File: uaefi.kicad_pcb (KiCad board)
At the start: 4 copper layers, 100 x 100 mm, 159 parts, among them J1 Conn_02x02_Odd_Even, J10 5569-16A2, J11 Conn_02x02_Odd_Even, J12 Conn_02x02_Odd_Even, J13 Conn_02x02_Odd_Even, J14 Conn_02x02_Odd_Even, J15 Conn_02x02_Odd_Even, J16 Conn_02x02_Odd_Even, J17 Conn_02x02_Odd_Even, J18 Conn_02x02_Odd_Even, J19 Conn_02x02_Odd_Even, J2 5569-20A2, J20 Conn_02x02_Odd_Even, J21 Conn_02x02_Odd_Even, J22 Conn_02x02_Odd_Even, J24 Conn_02x02_Odd_Even, J3 5569-06A2, J4 5569-08A2, J5 5569-18A2, J6 Conn_01x06, J7 Conn_01x05_Male, J8 USB_B_Mini, J9 USB_C, M1 Module-power_12and5V-0.2, M2 Module-knock-0.2, M3 Module-vr-discrete-0.5, M4 Module-vr-max9924-0.1, M5 Module-wbo-0.5, M6 Module:mega-mcu100/0.3, M7 Module-can-0.1, P1 Pad, P15 Pad, P16 Pad, P17 Pad, P18 Pad, P2 Pad, P3 Pad, P4 Pad, P5 Pad, P6 Pad, P7 Pad, P8 Pad, Q10 ISL9V3040D3ST, Q11 ISL9V3040D3ST, Q12 ISL9V3040D3ST, Q7 ISL9V3040D3ST, Q8 ISL9V3040D3ST, Q9 ISL9V3040D3ST, U1 TLE9201SG, U10 VNLD5160TR-E, U11 VNLD5160TR-E, U2 TLE9201SG, U3 MPX4/MPXH6400_MAP, U4 MAX31855KASA, U5 JDY-33, U6 VNLD5160TR-E, U7 VNLD5160TR-E, U8 VNLD5160TR-E, U9 VNLD5160TR-E

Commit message: Prepared the PCB for changes.
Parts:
- removed R5: 0, hellen-one-common:R0603
- moved R29 127.4 mm to (-25.3, 217.7)
- moved R31 127.4 mm to (-27.0, 217.7)
- moved R34 127.4 mm to (-23.6, 217.7)
- moved U10 127.4 mm to (-26.4, 200.0)
- moved U11 127.4 mm to (-26.4, 208.6)
- moved U9 127.4 mm to (-26.4, 191.2)
- moved R30 126.1 mm to (-15.1, 209.1)
- moved R32 126.1 mm to (-17.4, 206.8)
- moved R33 126.1 mm to (-19.2, 207.2)
- moved U5 122.7 mm to (265.2, 145.0)
- moved F10 121.4 mm to (28.9, 189.8)
- moved P7 116.8 mm to (249.4, 148.0)
- moved P8 116.8 mm to (249.4, 152.7)
- moved C27 112.7 mm to (223.0, 76.6)
- moved U3 105.7 mm to (230.2, 78.0)
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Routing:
- net +12V_RAW: track 250.7 -> 0.00 mm, vias 2 -> 0
- net +5VP: track 199.7 -> 0.00 mm, vias 3 -> 0
- net +5VA: track 171.8 -> 0.00 mm, vias 6 -> 0
- net +3.3VA: track 169.4 -> 0.00 mm, vias 5 -> 0
- net GNDA: track 155.8 -> 0.00 mm, vias 5 -> 0
- net /LS_HOT1: track 140.6 -> 0.13 mm, vias 2 -> 0
- net /LS_HOT2: track 138.9 -> 0.00 mm, vias 2 -> 0
- net /EGT/SPI_CS: track 111.5 -> 0.00 mm, vias 1 -> 0
- net /IN_BUTTON3: track 109.6 -> 0.00 mm, vias 1 -> 0
- net +3.3V: track 108.0 -> 0.00 mm, vias 8 -> 0
- net /EGT/SPI_SCK: track 107.3 -> 0.00 mm, vias 1 -> 0
- net /EGT/SPI_SO: track 104.7 -> 0.00 mm, vias 1 -> 0
- net /CAN+: track 102.6 -> 0.00 mm
- net /CAN-: track 100.8 -> 0.00 mm
- net /INJ1: track 89.1 -> 0.00 mm, vias 3 -> 0
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- removed copper zone on B.Cu, net /DC Driver 1/PWR
- removed copper zone on B.Cu, net /DC Driver 2/PWR
- removed copper zone on B.Cu, net GND
- removed copper zone on F.Cu, net GND
- removed copper zone on In1.Cu, net GND
- removed copper zone on In2.Cu, net GND
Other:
- board size 100 x 100 mm -> 150 x 120 mm
- copper layers 4 -> 2
- board text removed: "Always looking for C/C++/PHP/Java developers https://rusefi.com/s/mission"
- board text removed: "COMMUNITY SUPPORT ECU"
- board text removed: "G"
- board text removed: "https://rusefi.com/s/uaefi"

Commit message: tyring to make the pcb a two layer board
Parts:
- added R5: 0, hellen-one-common:R0603, F.Cu at (114.0, 88.0)
- BT1, D2, D4, R12, R13, R15, R16, U6, U8: moved to F.Cu
- moved U9 132.9 mm to (54.6, 85.9)
- moved U10 132.9 mm to (54.6, 94.6)
- moved R34 132.8 mm to (61.0, 115.3), turned to -90 degrees
- moved U11 132.7 mm to (54.6, 103.5)
- moved R31 132.5 mm to (57.1, 115.3), turned to -90 degrees
- moved R29 129.8 mm to (54.6, 115.3), turned to -90 degrees
- moved R33 121.1 mm to (59.7, 115.3)
- moved R32 118.8 mm to (58.4, 115.3)
- moved R30 117.5 mm to (55.9, 115.3), turned to -90 degrees
- moved C27 91.2 mm to (132.0, 83.0), turned to 0 degrees
- moved F10 90.4 mm to (84.5, 118.5)
- moved F5 90.4 mm to (84.5, 90.5)
- moved F6 90.4 mm to (84.5, 83.5)
- moved F7 90.4 mm to (84.6, 97.5)
- moved F8 90.4 mm to (84.6, 104.5)
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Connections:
- J20 pad 3: /OUT_IGN5 -> /OUT_IGN3
- J21 pad 1: /OUT_IGN3 -> /OUT_IGN4
- J21 pad 3: /OUT_IGN4 -> /OUT_IGN5
- J5 pad 11: /OUT_IGN4 -> /OUT_IGN5
- J5 pad 12: /OUT_IGN3 -> /OUT_IGN4
- J5 pad 13: /OUT_IGN5 -> /OUT_IGN3
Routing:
- net /INJ1: track 0.00 -> 120.2 mm, vias 0 -> 2
- net /INJ2: track 0.00 -> 119.7 mm, vias 0 -> 2
- net /INJ4: track 0.00 -> 108.5 mm, vias 0 -> 2
- net /INJ3: track 0.35 -> 108.7 mm, vias 0 -> 2
- net /INJ5: track 0.00 -> 98.0 mm, vias 0 -> 2
- net /INJ6: track 0.14 -> 95.4 mm, vias 0 -> 2
- net /OUT_DC2+: track 0.00 -> 27.8 mm
- net /OUT_DC1+: track 0.00 -> 24.9 mm, vias 0 -> 2
- net /OUT_DC2-: track 0.00 -> 22.2 mm, vias 0 -> 2
- net +12V: track 0.00 -> 21.1 mm
- net /12V_KEY: track 0.00 -> 20.8 mm
- net /DC Driver 1/PWR: track 0.00 -> 14.5 mm, vias 0 -> 2
- net /OUT_IGN6: track 0.00 -> 12.3 mm
- net /OUT_IGN2: track 0.00 -> 11.4 mm
- net /OUT_IGN5: track 0.00 -> 10.8 mm
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- added copper zone on B.Cu, net /DC Driver 1/PWR
- added copper zone on B.Cu, net /DC Driver 2/PWR
- added copper zone on F.Cu, net /OUT_IGN1
- added copper zone on F.Cu, net /OUT_IGN3
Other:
- board text removed: "UAEFI rev. D"

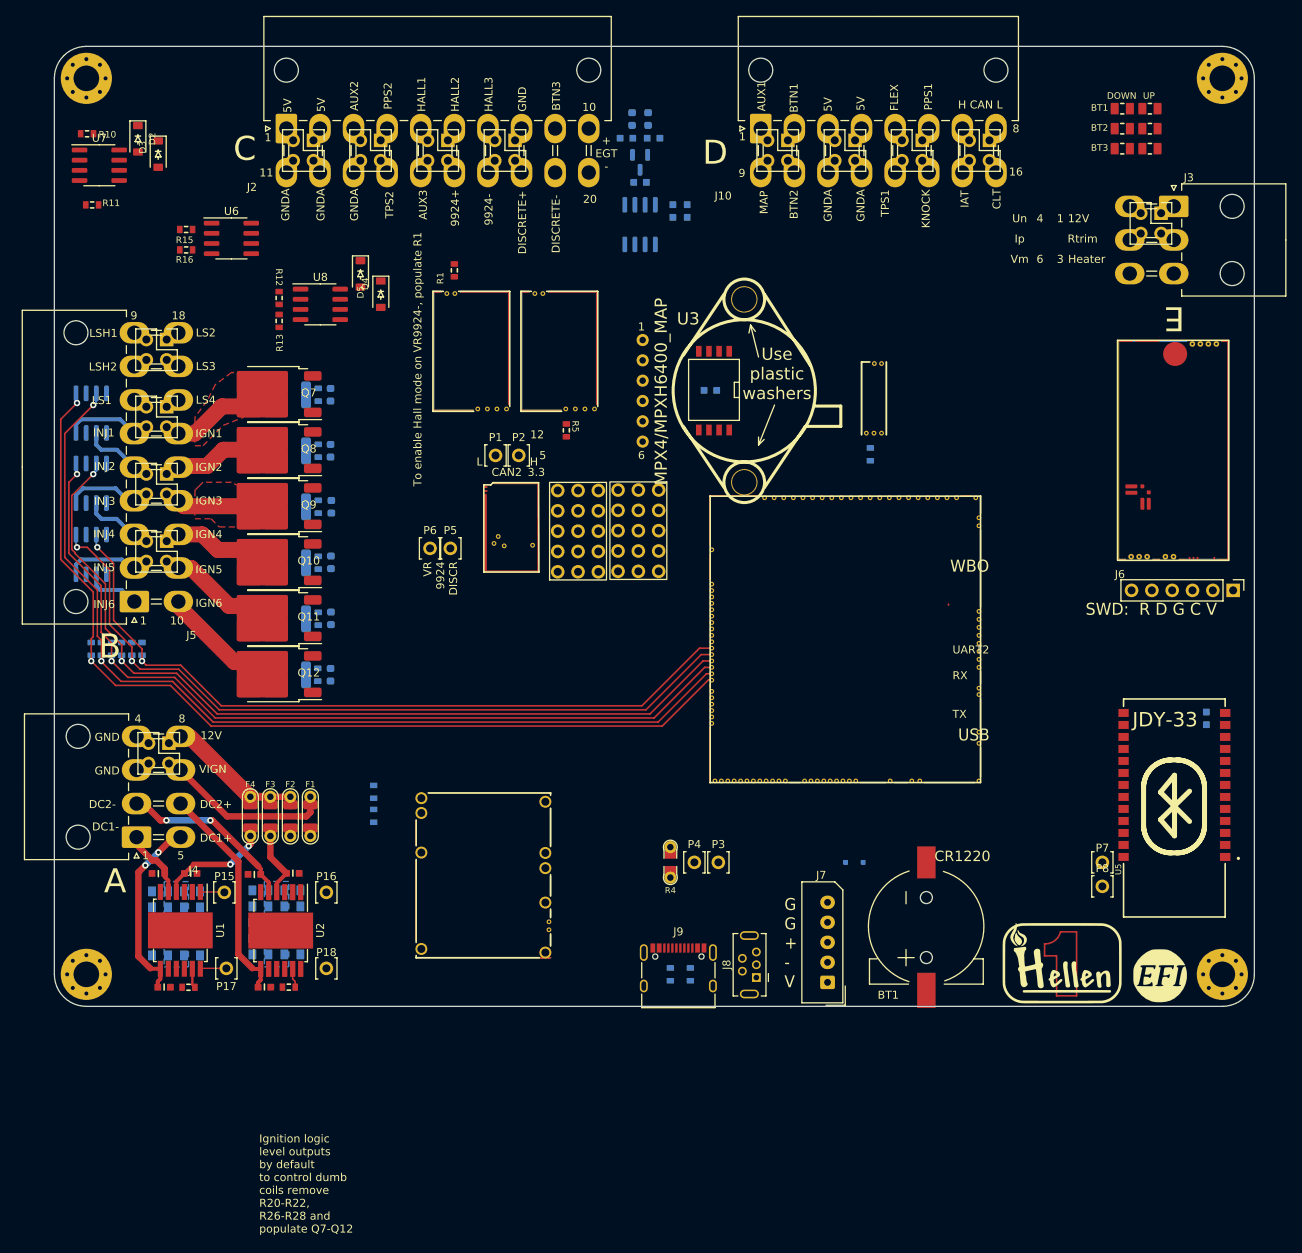
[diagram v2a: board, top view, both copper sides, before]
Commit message: Went back to the previous 4 layer board!
Mostly because i have found a way to make the boards abroad.
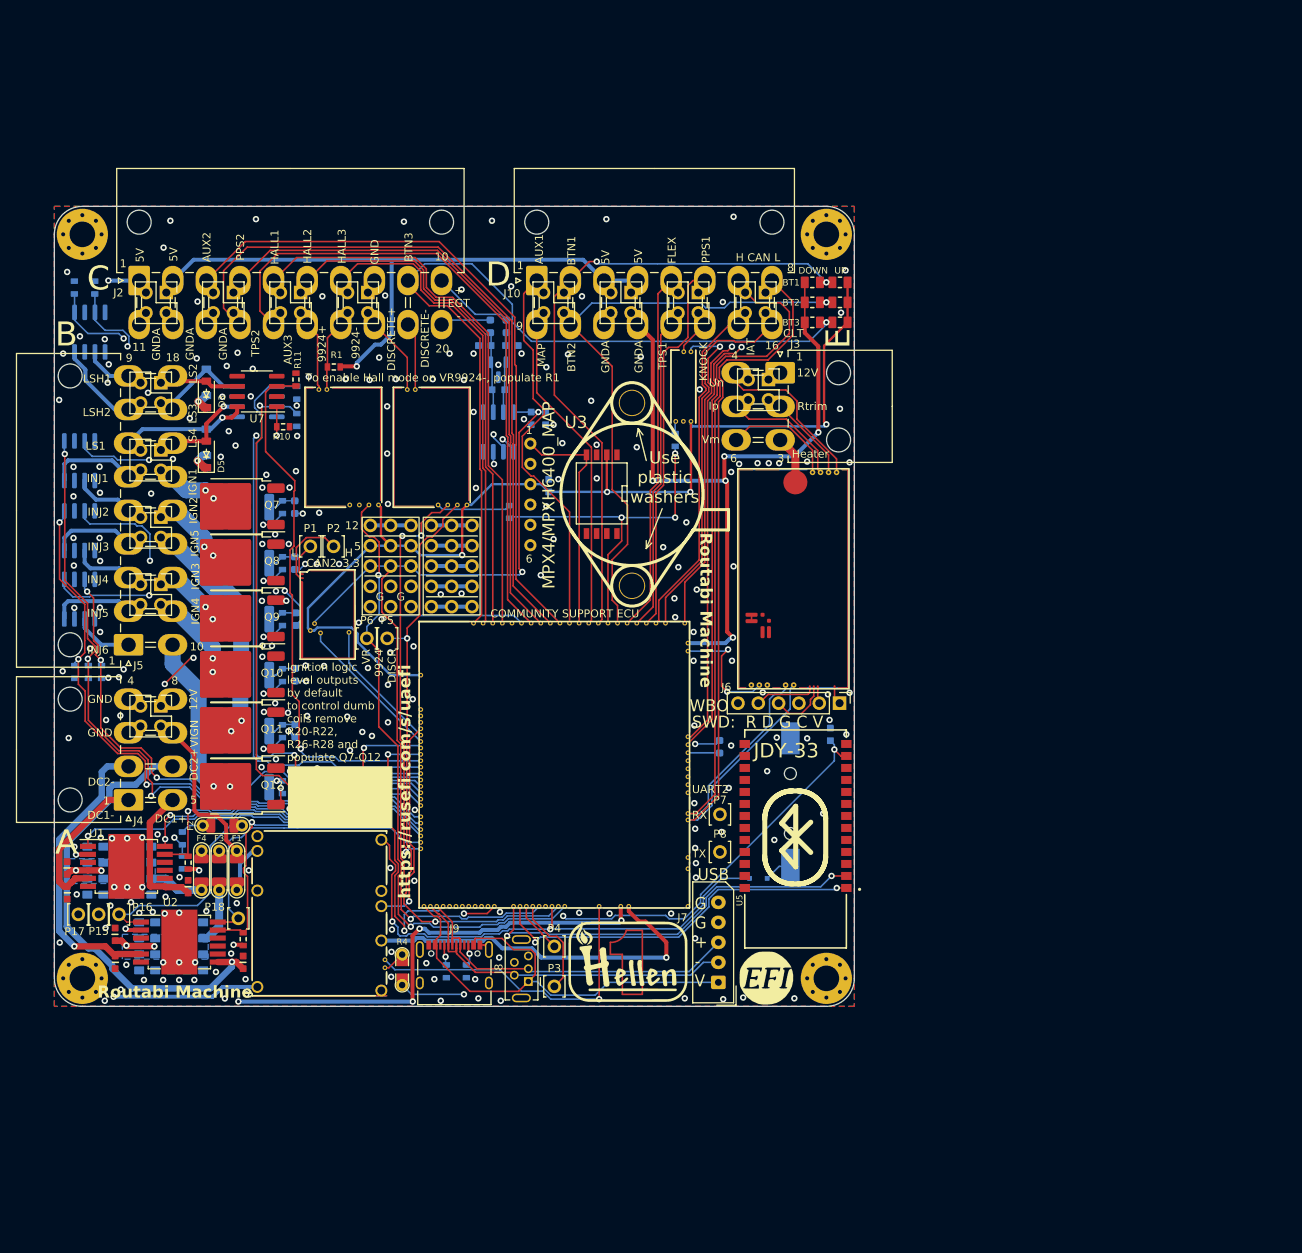
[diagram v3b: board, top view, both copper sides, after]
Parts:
- BT1, D2, D4, R12, R13, R15, R16, R5, U6, U8: moved to B.Cu
- moved G2 54.3 mm to (122.0, 154.5)
- moved J3 53.4 mm to (140.7, 80.8)
- moved J24 53.3 mm to (139.3, 81.7)
- moved H4 53.2 mm to (146.5, 63.5)
- moved J6 51.2 mm to (148.2, 122.1)
- moved M5 50.1 mm to (149.4, 120.4)
- moved H3 49.5 mm to (146.5, 156.5)
- moved F10 49.5 mm to (133.2, 127.5)
- moved G1 49.2 mm to (139.0, 156.5)
- moved P7 48.2 mm to (133.2, 136.0)
- moved P8 48.0 mm to (133.2, 140.7)
- moved U5 47.5 mm to (142.7, 138.9)
- moved C33 47.0 mm to (147.0, 126.0)
- moved R35 44.4 mm to (144.8, 69.5)
- moved R36 44.4 mm to (144.8, 72.0)
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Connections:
- J20 pad 3: /OUT_IGN3 -> /OUT_IGN5
- J21 pad 1: /OUT_IGN4 -> /OUT_IGN3
- J21 pad 3: /OUT_IGN5 -> /OUT_IGN4
- J5 pad 11: /OUT_IGN5 -> /OUT_IGN4
- J5 pad 12: /OUT_IGN4 -> /OUT_IGN3
- J5 pad 13: /OUT_IGN3 -> /OUT_IGN5
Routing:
- net +12V_RAW: track 1.00 -> 250.7 mm, vias 0 -> 2
- net +5VP: track 0.00 -> 199.7 mm, vias 0 -> 3
- net +5VA: track 0.00 -> 171.8 mm, vias 0 -> 6
- net +3.3VA: track 0.00 -> 169.4 mm, vias 0 -> 5
- net GNDA: track 0.00 -> 155.8 mm, vias 0 -> 5
- net /LS_HOT1: track 0.00 -> 140.6 mm, vias 0 -> 2
- net /LS_HOT2: track 0.13 -> 138.9 mm, vias 0 -> 2
- net /EGT/SPI_CS: track 0.00 -> 111.5 mm, vias 0 -> 1
- net /IN_BUTTON3: track 0.00 -> 109.6 mm, vias 0 -> 1
- net +3.3V: track 0.00 -> 108.0 mm, vias 0 -> 8
- net /EGT/SPI_SCK: track 0.00 -> 107.3 mm, vias 0 -> 1
- net /EGT/SPI_SO: track 0.00 -> 104.7 mm, vias 0 -> 1
- net /CAN+: track 0.00 -> 102.6 mm
- net /CAN-: track 0.00 -> 100.8 mm
- net /IN_TPS2: track 0.00 -> 88.5 mm
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- added copper zone on B.Cu, net GND
- added copper zone on F.Cu, net GND
- added copper zone on In1.Cu, net GND
- added copper zone on In2.Cu, net GND
- removed copper zone on F.Cu, net /OUT_IGN1
- removed copper zone on F.Cu, net /OUT_IGN3
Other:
- board size 150 x 120 mm -> 100 x 100 mm
- copper layers 2 -> 4
- board text added: "COMMUNITY SUPPORT ECU"
- board text added: "G"
- board text added: "Routabi Machine"
- board text added: "https://rusefi.com/s/uaefi"
